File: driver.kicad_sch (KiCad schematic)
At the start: 5 parts, among them U1 TLC5925IPWR

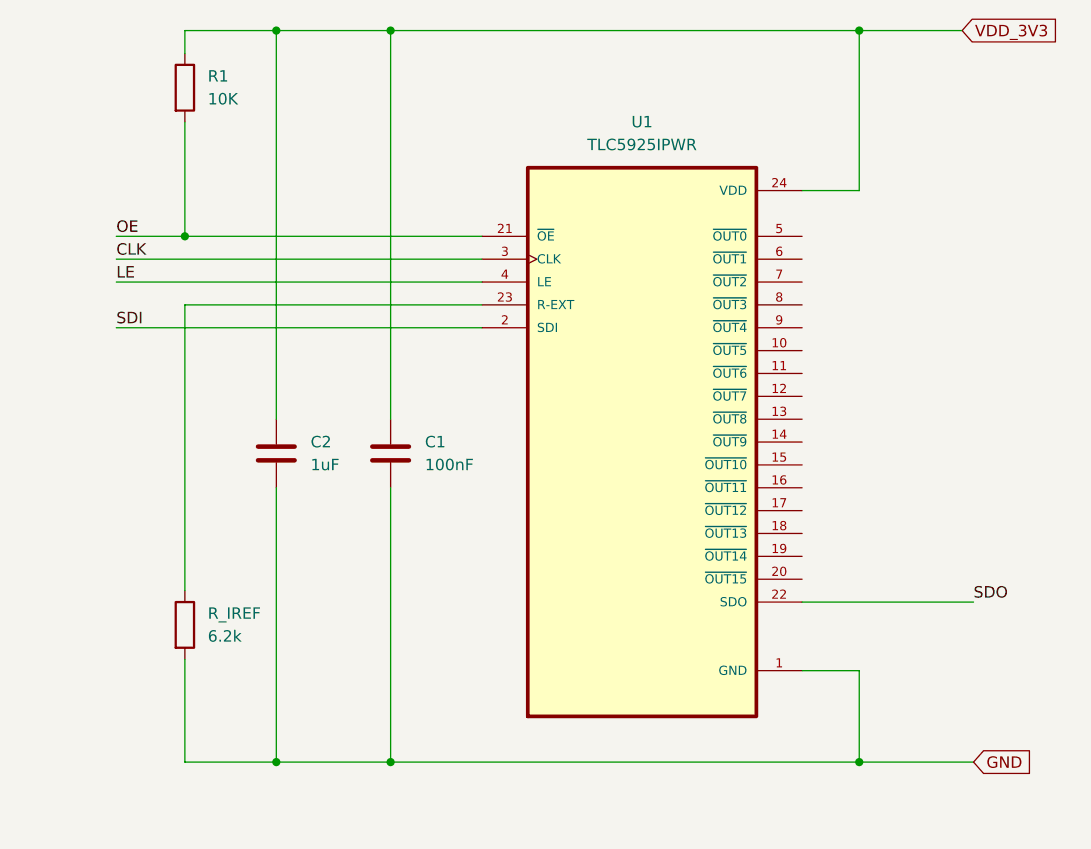
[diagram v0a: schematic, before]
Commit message: Place the 12 LEDs in one straight line at 10 mm pitch.
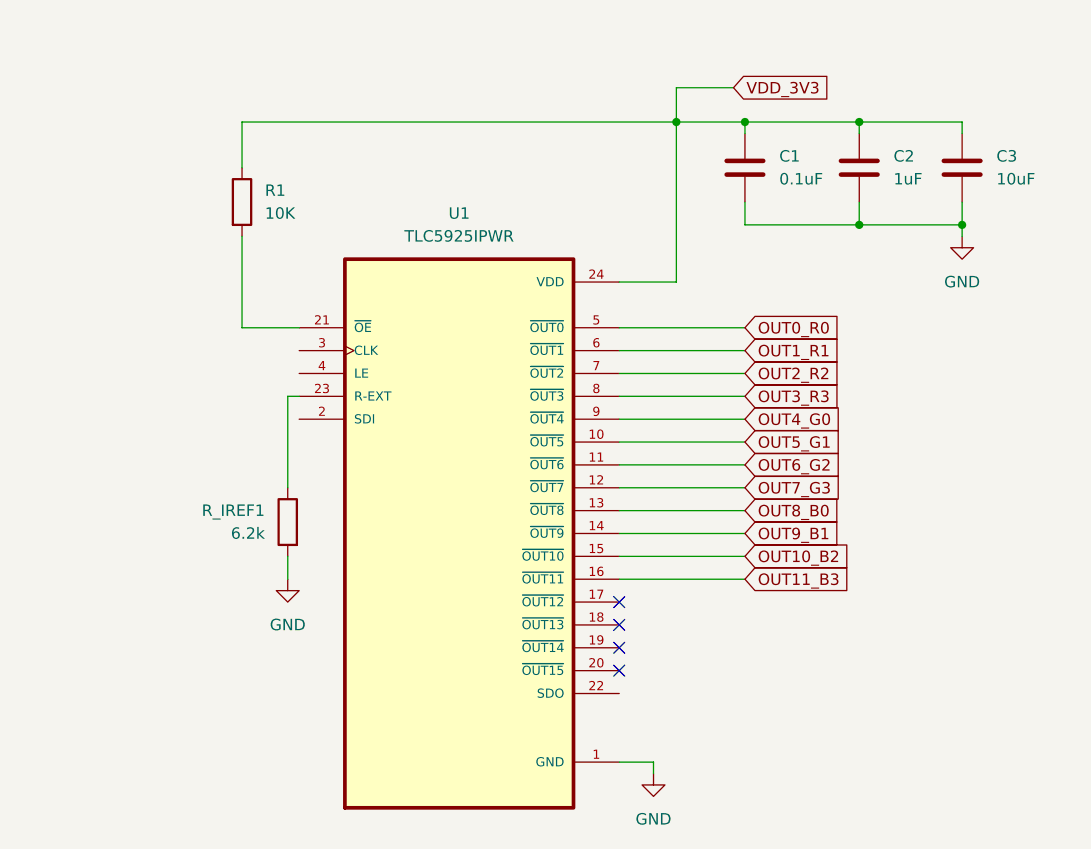
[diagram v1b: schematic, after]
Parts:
- added C1: 0.1uF, Capacitor_SMD:C_0603_1608Metric_Pad1.08x0.95mm_HandSolder, symbol Device:C
- C2: footprint (none) -> Capacitor_SMD:C_1206_3216Metric_Pad1.33x1.80mm_HandSolder
- C3: renamed from C1; value 100nF -> 10uF; footprint (none) -> Capacitor_SMD:C_0805_2012Metric_Pad1.18x1.45mm_HandSolder
- R1: footprint (none) -> Resistor_SMD:R_1206_3216Metric_Pad1.30x1.75mm_HandSolder
- R_IREF1: renamed from R_IREF; footprint (none) -> Resistor_SMD:R_1206_3216Metric_Pad1.30x1.75mm_HandSolder
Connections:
- net GND: now also C1.2
- net VDD_3V3: now also C1.1
- net OUT5_G1: now reaches U1.10 (~{OUT5})
- net OUT6_G2: now reaches U1.11 (~{OUT6})
- net OUT7_G3: now reaches U1.12 (~{OUT7})
- net OUT8_B0: now reaches U1.13 (~{OUT8})
- net OUT9_B1: now reaches U1.14 (~{OUT9})
- net OUT10_B2: now reaches U1.15 (~{OUT10})
- net OUT11_B3: now reaches U1.16 (~{OUT11})
- net OUT0_R0: now reaches U1.5 (~{OUT0})
- net OUT1_R1: now reaches U1.6 (~{OUT1})
- net OUT2_R2: now reaches U1.7 (~{OUT2})
- net OUT3_R3: now reaches U1.8 (~{OUT3})
- net OUT4_G0: now reaches U1.9 (~{OUT4})
- net CLK: no longer names the net of U1.3 (CLK)
- net LE: no longer names the net of U1.4 (LE)
- net OE: no longer names the net of R1.2, U1.21 (~{OE})
- net SDI: no longer names the net of U1.2 (SDI)
- net SDO: no longer names the net of U1.22 (SDO)
- no-connect marks 0 -> 4
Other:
- moved on the sheet: C2, C3, R1, R_IREF1, U1

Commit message: v0 2 layer needs grounding islands
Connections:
- net SDI: now reaches U1.2 (SDI)
- net OE: now reaches R1.2, U1.21 (~{OE})
- net SDO: now reaches U1.22 (SDO)
- net CLK: now reaches U1.3 (CLK)
- net LE: now reaches U1.4 (LE)
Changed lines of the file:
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@@
 	(paper "A4")
+	(junction
+		(at 109.22 68.58)
+		(diameter 0)
+		(color 0 0 0 0)
+	)
 	(junction
 		(at 177.8 45.72)
@@
 	(wire
 		(pts
+			(xy 113.03 73.66) (xy 115.57 73.66)
+		)
+		(stroke
+			(width 0)
+			(type default)
+		)
+	)
+	(wire
+		(pts
+			(xy 111.76 73.66) (xy 111.76 71.12)
+		)
+		(stroke
+			(width 0)
+			(type default)
+		)
+	)
+	(wire
+		(pts
+			(xy 91.44 71.12) (xy 109.22 71.12)
+		)
+		(stroke
+			(width 0)
+			(type default)
+		)
+	)
+	(wire
+		(pts
 			(xy 157.48 41.91) (xy 157.48 45.72)
 		)
@@
 	(wire
 		(pts
+			(xy 91.44 78.74) (xy 115.57 78.74)
+		)
+		(stroke
+			(width 0)
+			(type default)
+		)
+	)
+	(wire
+		(pts
+			(xy 151.13 109.22) (xy 171.45 109.22)
+		)
+		(stroke
+			(width 0)
+			(type default)
+		)
+	)
+	(wire
+		(pts
 			(xy 151.13 93.98) (xy 165.1 93.98)
 		)
@@
 	(wire
 		(pts
+			(xy 113.03 76.2) (xy 113.03 73.66)
+		)
+		(stroke
+			(width 0)
+			(type default)
+		)
+	)
+	(wire
+		(pts
+			(xy 111.76 71.12) (xy 115.57 71.12)
+		)
+		(stroke
+			(width 0)
+			(type default)
+		)
+	)
+	(wire
+		(pts
 			(xy 165.1 46.99) (xy 165.1 45.72)
 		)
@@
 	(wire
 		(pts
+			(xy 109.22 71.12) (xy 109.22 68.58)
+		)
+		(stroke
+			(width 0)
+			(type default)
+		)
+	)
+	(wire
+		(pts
 			(xy 151.13 73.66) (xy 165.1 73.66)
 		)
@@
 	(wire
 		(pts
+			(xy 91.44 73.66) (xy 111.76 73.66)
+		)
+		(stroke
+			(width 0)
+			(type default)
+		)
+	)
+	(wire
+		(pts
 			(xy 115.57 76.2) (xy 114.3 76.2)
 		)
@@
 	(wire
 		(pts
+			(xy 91.44 76.2) (xy 113.03 76.2)
+		)
+		(stroke
+			(width 0)
+			(type default)
+		)
+	)
+	(wire
+		(pts
 			(xy 154.94 116.84) (xy 151.13 116.84)
 		)
@@
 		)
 	)
+	(global_label "CLK"
+		(shape input)
+		(at 91.44 73.66 180)
+		(fields_autoplaced yes)
+		(effects
+			(font
+				(size 1.27 1.27)
+			)
+			(justify right)
+		)
+		(property "Intersheetrefs" "${INTERSHEET_REFS}"
+			(at 84.8867 73.66 0)
+			(hide yes)
+			(show_name no)
+			(do_not_autoplace no)
+			(effects
+				(font
+					(size 1.27 1.27)
+				)
+				(justify right)
+			)
+		)
+	)
 	(global_label "OUT9_B1"
 		(shape input)
@@
 		)
 	)
+	(global_label "LE"
+		(shape input)
+		(at 91.44 76.2 180)
+		(fields_autoplaced yes)
+		(effects
+			(font
+				(size 1.27 1.27)
+			)
+			(justify right)
+		)
+		(property "Intersheetrefs" "${INTERSHEET_REFS}"
+			(at 86.2777 76.2 0)
+			(hide yes)
+			(show_name no)
+			(do_not_autoplace no)
+			(effects
+				(font
+					(size 1.27 1.27)
+				)
+				(justify right)
+			)
+		)
+	)
 	(global_label "VDD_3V3"
 		(shape input)
@@
 		)
 	)
+	(global_label "SDO"
+		(shape input)
+		(at 171.45 109.22 0)
+		(fields_autoplaced yes)
+		(effects
+			(font
+				(size 1.27 1.27)
+			)
+			(justify left)
+		)
+		(property "Intersheetrefs" "${INTERSHEET_REFS}"
+			(at 178.2452 109.22 0)
+			(hide yes)
+			(show_name no)
+			(do_not_autoplace no)
+			(effects
+				(font
+					(size 1.27 1.27)
+				)
+				(justify left)
+			)
+		)
+	)
 	(global_label "OUT7_G3"
 		(shape input)
@@
 		)
 	)
+	(global_label "OE"
+		(shape input)
+		(at 91.44 71.12 180)
+		(fields_autoplaced yes)
+		(effects
+			(font
+				(size 1.27 1.27)
+			)
+			(justify right)
+		)
+		(property "Intersheetrefs" "${INTERSHEET_REFS}"
+			(at 85.9753 71.12 0)
+			(hide yes)
+			(show_name no)
+			(do_not_autoplace no)
+			(effects
+				(font
+					(size 1.27 1.27)
+				)
+				(justify right)
+			)
+		)
+	)
 	(global_label "OUT10_B2"
 		(shape input)
@@
 			)
 		)
+	)
+	(global_label "SDI"
+		(shape input)
+		(at 91.44 78.74 180)
+		(fields_autoplaced yes)
+		(effects
+			(font
+				(size 1.27 1.27)
+			)
+			(justify right)
+		)
+		(property "Intersheetrefs" "${INTERSHEET_REFS}"
+			(at 85.3705 78.74 0)
+			(hide yes)
+			(show_name no)
+			(do_not_autoplace no)
+			(effects
+				(font
+					(size 1.27 1.27)
+				)
+				(justify right)
+			)
+		)
